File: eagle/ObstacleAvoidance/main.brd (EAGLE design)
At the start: 115 x 70 mm, 19 parts, among them IC1 L293D, X1 JST-XH-02-PIN-LONG-PAD, X2 JST-XH-02-PIN-LONG-PAD, X3 JST-XH-04-PIN-LONG-PAD

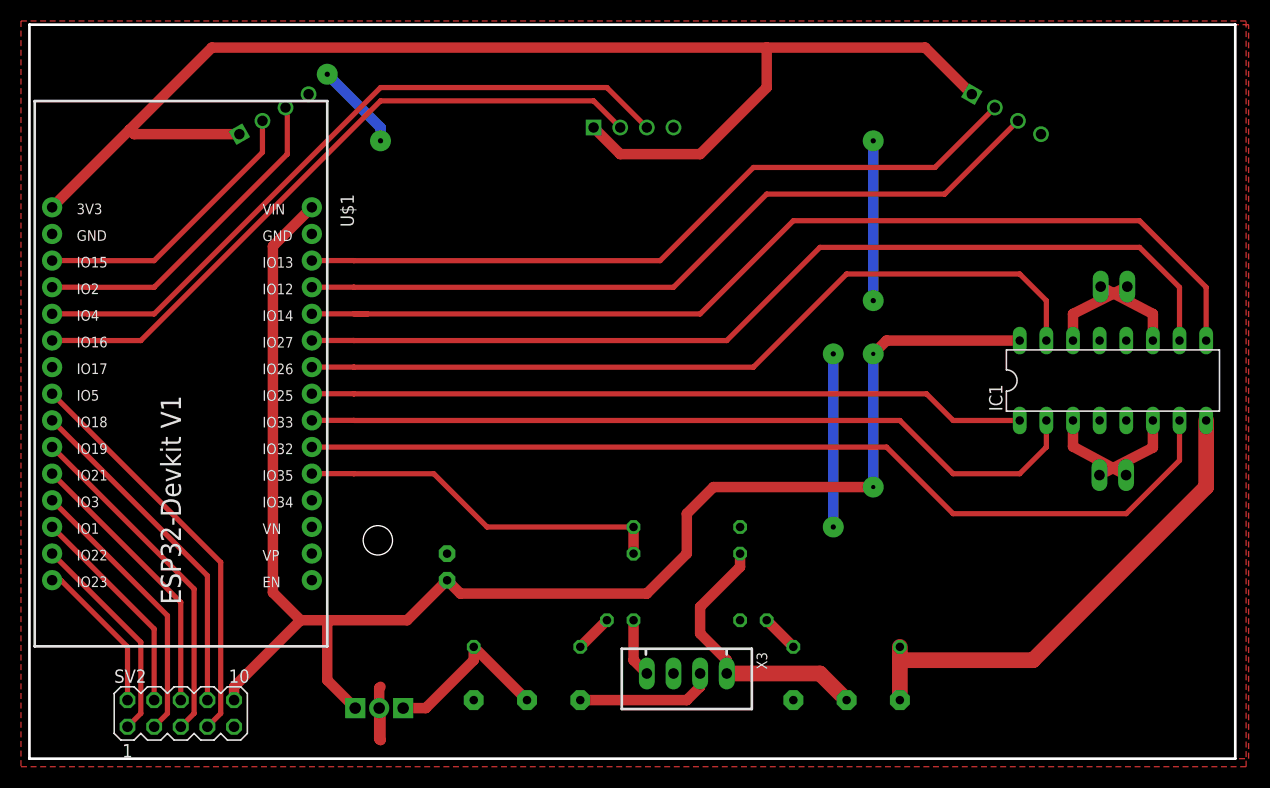
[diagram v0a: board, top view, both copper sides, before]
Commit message: Feat: New PCB routing
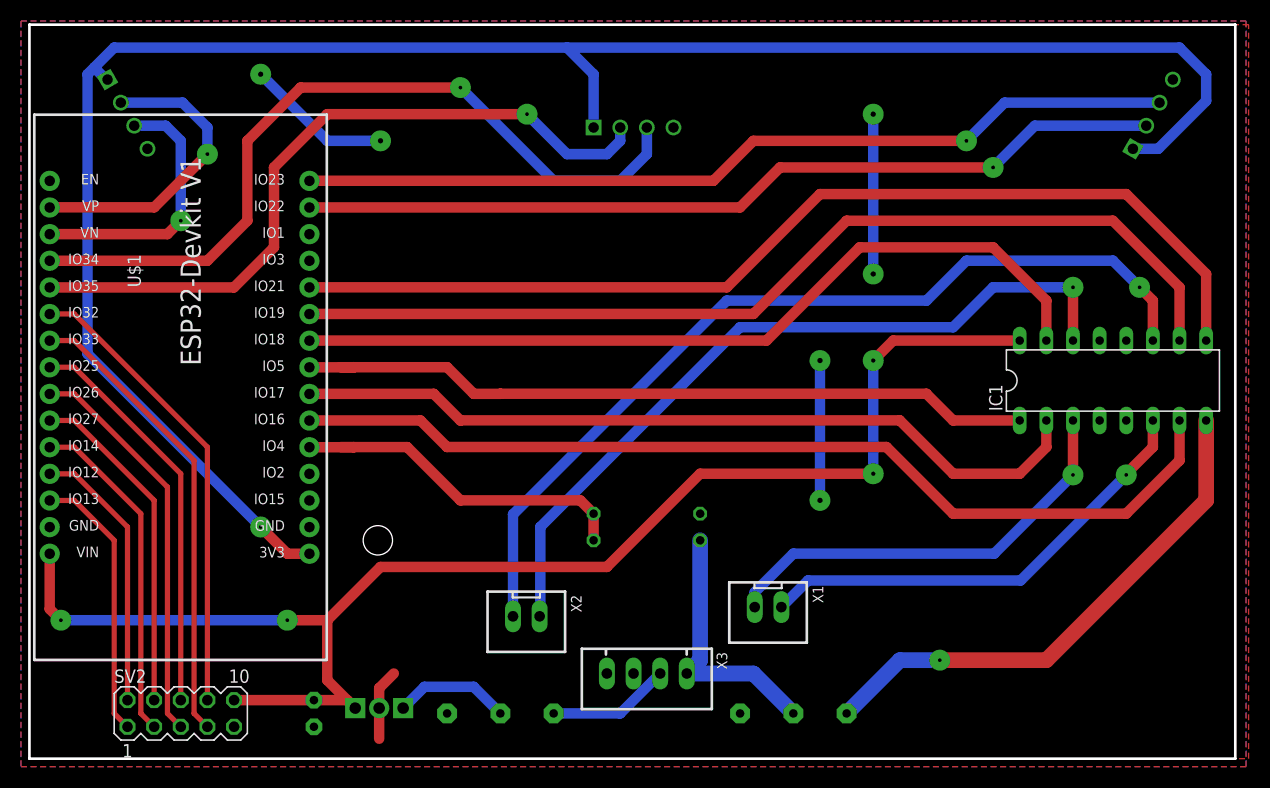
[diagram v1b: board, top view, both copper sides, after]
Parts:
- removed LED1, LED2: TLLG4400, led:LED3MM
- removed R3, R4: 1k, rcl:0207/10
- moved X2 64.3 mm to (69.8, 25.8), flipped to the top, turned to 180 degrees
- moved X1 35.2 mm to (92.8, 26.7), flipped to the top
- moved C2 18.9 mm to (49.5, 16.5), turned to 270 degrees
- moved U$2 14.0 mm to (129.5, 73.7), turned to 120 degrees
- moved U$3 14.0 mm to (31.8, 73.7), turned to 240 degrees
- moved U$1 13.0 mm to (35.6, 54.6), turned to 90 degrees
- moved J2 5.24 mm to (92.7, 16.5)
- moved R1 4.02 mm to (81.3, 35.6)
- moved R2 4.02 mm to (81.3, 33.0)
- moved X3 3.81 mm to (81.3, 20.3)
- moved J1 2.84 mm to (64.8, 16.5)
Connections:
- removed net N$15: U$1.7
- removed net N$5: LED1.A, R4.1
- removed net N$9: LED2.A, R3.2
- net 12V-VCC2: no longer R3.1
- net 8V-1: no longer R4.2
- net ECHO-F: now also U$1.19; no longer U$1.5
- net ECHO-L: now also U$1.18; no longer U$1.4
- net ECHO-R: now also U$1.15; no longer U$1.27
- net GND: no longer LED1.K, LED2.K
- net IN1-A: now also U$1.10; no longer U$1.25
- net IN1-B: now also U$1.6; no longer U$1.21
- net IN2-A: now also U$1.9; no longer U$1.24
- net IN2-B: now also U$1.7; no longer U$1.22
- net OUT1: now also U$1.27; no longer U$1.15
- net OUT2: now also U$1.28; no longer U$1.14
- net OUT3: now also U$1.25; no longer U$1.13
- net OUT4: now also U$1.26; no longer U$1.12
- net OUT5: now also U$1.23; no longer U$1.11
- net OUT6: now also U$1.24; no longer U$1.10
- net OUT7: now also U$1.21; no longer U$1.9
- net OUT8: now also U$1.22; no longer U$1.8
- net PWM-A: now also U$1.11; no longer U$1.26
- net PWM-B: now also U$1.8; no longer U$1.23
- net TRIG-F: now also U$1.20; no longer U$1.6
- net TRIG-L: now also U$1.17; no longer U$1.3
- net TRIG-R: now also U$1.14; no longer U$1.28
- net VOLT: now also U$1.5; no longer U$1.20
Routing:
- net N$4: track 8.16 -> 86.2 mm, vias 0 -> 1
- net N$3: track 8.34 -> 73.9 mm, vias 0 -> 1
- net 3.3V: track 130.5 -> 186.3 mm, vias 0 -> 1
- net N$2: track 8.32 -> 44.4 mm, vias 0 -> 1
- net N$1: track 8.24 -> 41.6 mm, vias 0 -> 1
- net 5V: track 152.1 -> 137.0 mm, vias 2 -> 4
- net TRIG-R: track 71.2 -> 83.0 mm, vias 0 -> 1
- net OUT3: track 20.6 -> 32.2 mm
- net OUT5: track 26.7 -> 38.3 mm
- net OUT7: track 32.8 -> 44.4 mm
- net OUT1: track 14.9 -> 26.0 mm
- net ECHO-R: track 73.9 -> 84.2 mm, vias 0 -> 1
- net ECHO-F: track 67.2 -> 75.5 mm, vias 0 -> 1
- net ECHO-L: track 32.2 -> 25.7 mm, vias 0 -> 1
- net 8V-1: track 17.1 -> 11.2 mm
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- added copper zone on layer 16, net GND

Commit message: Feat: Swap bottom-top
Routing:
- net IN2-B: track 77.0 -> 74.2 mm
- net 5V: track 137.0 -> 134.5 mm
- net N$3: track 73.9 -> 75.6 mm
- net 8V: track 11.7 -> 13.2 mm
- net OUT6: track 38.3 -> 36.9 mm
- net OUT3: track 32.2 -> 30.8 mm
- net OUT4: track 32.2 -> 30.8 mm
- net OUT2: track 26.0 -> 24.7 mm
- net OUT1: track 26.0 -> 24.7 mm
- net OUT7: track 44.4 -> 43.0 mm
- net OUT5: track 38.3 -> 36.9 mm
- net OUT8: track 44.4 -> 43.0 mm
- net PWM-B: track 71.1 -> 69.8 mm
- net VOLT: track 33.5 -> 32.3 mm
- net IN1-B: track 92.6 -> 91.5 mm
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
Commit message: Feat: 3D model and pcb changes
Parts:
- moved U$2 2.54 mm to (129.5, 76.2)
- moved U$3 2.54 mm to (31.8, 76.2)
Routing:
- net 3.3V: track 185.9 -> 190.8 mm
- net ECHO-L: track 25.7 -> 27.5 mm
- net ECHO-R: track 84.2 -> 86.0 mm
- net TRIG-R: track 83.0 -> 84.1 mm
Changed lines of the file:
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@@
 </layers>
 <board>
-<fusionsync huburn="a.YnVzaW5lc3M6Z21haWw0MzYwOTY" projecturn="a.YnVzaW5lc3M6Z21haWw0MzYwOTYjMjAxOTExMjUyNDE4MzY5NzY" f3durn="urn:adsk.wipprod:dm.lineage:NBSkxh8rSPakSfSzdT5ugQ" pcbguid="deb97233-5946-44c7-9ab5-95046c2ec4ee" lastpulledtime="2019-11-27T21:35:54Z" lastsyncedchangeguid="d6366f3e-85ad-fa97-e8cb-b64b5bb49a39"/>
+<fusionsync huburn="a.YnVzaW5lc3M6Z21haWw0MzYwOTY" projecturn="a.YnVzaW5lc3M6Z21haWw0MzYwOTYjMjAxOTExMjUyNDE4MzY5NzY" f3durn="urn:adsk.wipprod:dm.lineage:NBSkxh8rSPakSfSzdT5ugQ" pcbguid="deb97233-5946-44c7-9ab5-95046c2ec4ee" lastpulledtime="2019-11-29T17:32:53Z" lastsyncedchangeguid="fbe9b0a7-f74d-2411-8d66-78c79ab0fd07"/>
 <plain>
+<hole x="42.397" y="77.197" drill="4"/>
+<hole x="117.397" y="77.197" drill="4"/>
+<hole x="80" y="77.197" drill="4"/>
 <wire x1="22.397" y1="82.197" x2="22.397" y2="12.197" width="0.254" layer="20"/>
 <wire x1="22.397" y1="12.197" x2="137.397" y2="12.197" width="0.254" layer="20"/>
@@
 <attribute name="VALUE" x="118.237" y="47.625" size="1.27" layer="27" ratio="10"/>
 </element>
-<element name="U$2" library="diy-modules" package="ULTRASONIC-HC-SR04#V" value="ULTRASONIC-HC-SR04#V" x="129.54" y="73.66" smashed="yes" rot="MR120">
-<attribute name="NAME" x="125.690515625" y="75.88249375" size="1.27" layer="26" rot="MR120" align="bottom-center"/>
-<attribute name="VALUE" x="113.592140625" y="82.86749375" size="1.27" layer="28" rot="MR120" align="top-center"/>
-</element>
-<element name="U$3" library="diy-modules" package="ULTRASONIC-HC-SR04#V" value="ULTRASONIC-HC-SR04#V" x="31.75" y="73.66" smashed="yes" rot="MR240">
-<attribute name="NAME" x="30.10020625" y="72.7075" size="1.27" layer="26" rot="MR210" align="bottom-center"/>
-<attribute name="VALUE" x="47.69785" y="82.86749375" size="1.27" layer="28" rot="MR240" align="top-center"/>
+<element name="U$2" library="diy-modules" package="ULTRASONIC-HC-SR04#V" value="ULTRASONIC-HC-SR04#V" x="129.54" y="76.2" smashed="yes" rot="MR120">
+<attribute name="NAME" x="125.690515625" y="78.42249375" size="1.27" layer="26" rot="MR120" align="bottom-center"/>
+<attribute name="VALUE" x="113.592140625" y="85.40749375" size="1.27" layer="28" rot="MR120" align="top-center"/>
+</element>
+<element name="U$3" library="diy-modules" package="ULTRASONIC-HC-SR04#V" value="ULTRASONIC-HC-SR04#V" x="31.75" y="76.2" smashed="yes" rot="MR240">
+<attribute name="NAME" x="30.10020625" y="75.2475" size="1.27" layer="26" rot="MR210" align="bottom-center"/>
+<attribute name="VALUE" x="47.69785" y="85.40749375" size="1.27" layer="28" rot="MR240" align="top-center"/>
 </element>
 <element name="U$7" library="tango" package="L7805" value="-L7805" x="55.88" y="26.67" smashed="yes" rot="MR0">
@@
 <wire x1="102.87" y1="73.66" x2="102.87" y2="58.42" width="1" layer="1"/>
 <wire x1="97.79" y1="50.165" x2="97.79" y2="36.83" width="1" layer="1"/>
-<wire x1="127" y1="52.07" x2="131.445" y2="76.95955625" width="0" layer="19" extent="1-1"/>
-<wire x1="124.46" y1="52.07" x2="127" y2="52.07" width="0" layer="19" extent="1-1"/>
-<wire x1="127" y1="44.45" x2="127" y2="52.07" width="0" layer="19" extent="1-1"/>
-<wire x1="124.46" y1="44.45" x2="127" y2="44.45" width="0" layer="19" extent="1-1"/>
-<wire x1="102.87" y1="58.42" x2="124.46" y2="52.07" width="0" layer="19" extent="1-1"/>
-<wire x1="97.79" y1="50.165" x2="102.87" y2="58.42" width="0" layer="19" extent="1-1"/>
-<wire x1="86.36" y1="35.56" x2="97.79" y2="36.83" width="0" layer="19" extent="1-1"/>
-<wire x1="77.47" y1="20.32" x2="86.36" y2="35.56" width="0" layer="19" extent="1-1"/>
-<wire x1="83.82" y1="72.39" x2="102.87" y2="73.66" width="0" layer="19" extent="1-1"/>
-<wire x1="57.15" y1="20.32" x2="77.47" y2="20.32" width="0" layer="19" extent="1-1"/>
-<wire x1="49.53" y1="15.24" x2="55.753" y2="14.097" width="0" layer="19" extent="1-1"/>
-<wire x1="41.91" y1="15.24" x2="49.53" y2="15.24" width="0" layer="19" extent="1-1"/>
-<wire x1="24.33" y1="34.28" x2="41.91" y2="15.24" width="0" layer="19" extent="1-1"/>
-<wire x1="55.88" y1="71.12" x2="83.82" y2="72.39" width="0" layer="19" extent="1-1"/>
-<wire x1="33.655" y1="70.360440625" x2="44.45" y2="77.47" width="0" layer="19" extent="1-1"/>
 </signal>
 <signal name="5V">
@@
 <contactref element="U$8" pad="1"/>
 <via x="44.45" y="34.29" extent="1-16" drill="0.35" diameter="2"/>
-<wire x1="29.845" y1="76.95955625" x2="29.72044375" y2="76.95955625" width="1" layer="16"/>
+<wire x1="29.845" y1="79.49955625" x2="29.72044375" y2="79.49955625" width="1" layer="16"/>
 <wire x1="49.1" y1="31.74" x2="47" y2="31.74" width="1" layer="16"/>
 <wire x1="47" y1="31.74" x2="44.45" y2="34.29" width="1" layer="16"/>
 <wire x1="44.45" y1="34.29" x2="27.94" y2="50.8" width="1" layer="1"/>
-<wire x1="27.94" y1="50.8" x2="27.94" y2="77.47" width="1" layer="1"/>
-<wire x1="27.94" y1="77.47" x2="30.48" y2="80.01" width="1" layer="1"/>
-<wire x1="132.08" y1="80.01" x2="134.62" y2="77.47" width="1" layer="1"/>
-<wire x1="134.62" y1="77.47" x2="134.62" y2="73.66" width="1" layer="1"/>
-<wire x1="134.62" y1="73.66" x2="130.81" y2="69.85" width="1" layer="1"/>
-<wire x1="130.81" y1="69.85" x2="128.145440625" y2="69.85" width="1" layer="1"/>
-<wire x1="128.145440625" y1="69.85" x2="127.635" y2="70.360440625" width="1" layer="1"/>
-<wire x1="30.48" y1="80.01" x2="73.66" y2="80.01" width="1" layer="1"/>
-<wire x1="73.66" y1="80.01" x2="132.08" y2="80.01" width="1" layer="1"/>
-<wire x1="73.66" y1="80.01" x2="76.2" y2="77.47" width="1" layer="1"/>
+<wire x1="27.94" y1="77.47" x2="27.94" y2="50.8" width="1" layer="1"/>
+<wire x1="132.08" y1="81.28" x2="134.62" y2="78.74" width="1" layer="1"/>
+<wire x1="134.62" y1="78.74" x2="134.62" y2="76.2" width="1" layer="1"/>
+<wire x1="134.62" y1="76.2" x2="131.320440625" y2="72.900440625" width="1" layer="1"/>
+<wire x1="72.39" y1="81.28" x2="29.21" y2="81.28" width="1" layer="1"/>
+<wire x1="72.39" y1="81.28" x2="132.08" y2="81.28" width="1" layer="1"/>
+<wire x1="72.39" y1="81.28" x2="76.2" y2="77.47" width="1" layer="1"/>
 <wire x1="76.2" y1="77.47" x2="76.2" y2="72.39" width="1" layer="1"/>
-<wire x1="44.45" y1="34.29" x2="29.845" y2="76.95955625" width="0" layer="19" extent="1-1"/>
+<wire x1="27.877721875" y1="77.532278125" x2="27.94" y2="77.47" width="1" layer="1"/>
+<wire x1="29.21" y1="81.28" x2="27.877721875" y2="79.947721875" width="1" layer="1"/>
+<wire x1="29.845" y1="79.49955625" x2="27.877721875" y2="77.532278125" width="1" layer="1"/>
+<wire x1="27.877721875" y1="77.532278125" x2="27.877721875" y2="79.947721875" width="1" layer="1"/>
+<wire x1="127.635" y1="72.900440625" x2="131.320440625" y2="72.900440625" width="1" layer="1"/>
 </signal>
 <signal name="VOLT">
@@
 <wire x1="36.83" y1="63.5" x2="35.55" y2="62.22" width="1" layer="16"/>
 <wire x1="35.55" y1="62.22" x2="24.33" y2="62.22" width="1" layer="16"/>
-<wire x1="36.83" y1="63.5" x2="36.83" y2="71.12" width="1" layer="1"/>
-<wire x1="35.389853125" y1="72.560146875" x2="32.385" y2="72.560146875" width="1" layer="1"/>
-<wire x1="36.83" y1="71.12" x2="35.389853125" y2="72.560146875" width="1" layer="1"/>
+<wire x1="36.83" y1="63.5" x2="36.83" y2="66.04" width="1" layer="1"/>
+<wire x1="31.115" y1="73.830146875" x2="32.385" y2="75.100146875" width="1" layer="1"/>
+<wire x1="31.115" y1="73.830146875" x2="31.115" y2="71.755" width="1" layer="1"/>
+<wire x1="36.83" y1="66.04" x2="31.115" y2="71.755" width="1" layer="1"/>
 </signal>
 <signal name="TRIG-L">
@@
 <wire x1="24.33" y1="64.76" x2="34.28" y2="64.76" width="1" layer="16"/>
 <wire x1="34.28" y1="64.76" x2="39.37" y2="69.85" width="1" layer="16"/>
-<wire x1="31.115" y1="74.75985" x2="37.00015" y2="74.75985" width="1" layer="1"/>
-<wire x1="39.37" y1="72.39" x2="39.37" y2="69.85" width="1" layer="1"/>
-<wire x1="37.00015" y1="74.75985" x2="39.37" y2="72.39" width="1" layer="1"/>
+<wire x1="31.115" y1="77.29985" x2="33.19015" y2="77.29985" width="1" layer="1"/>
+<wire x1="39.37" y1="71.12" x2="39.37" y2="69.85" width="1" layer="1"/>
+<wire x1="39.37" y1="71.12" x2="33.19015" y2="77.29985" width="1" layer="1"/>
 </signal>
 <signal name="ECHO-R">
@@
 <wire x1="87.62" y1="67.3" x2="91.44" y2="71.12" width="1" layer="16"/>
 <wire x1="91.44" y1="71.12" x2="111.76" y2="71.12" width="1" layer="16"/>
-<wire x1="111.76" y1="71.12" x2="115.39985" y2="74.75985" width="1" layer="1"/>
-<wire x1="115.39985" y1="74.75985" x2="130.175" y2="74.75985" width="1" layer="1"/>
+<wire x1="113.03" y1="73.66" x2="111.76" y2="72.39" width="1" layer="1"/>
+<wire x1="111.76" y1="71.12" x2="111.76" y2="72.39" width="1" layer="1"/>
+<wire x1="130.175" y1="77.29985" x2="127.472225" y2="77.29985" width="1" layer="1"/>
+<wire x1="123.832375" y1="73.66" x2="113.03" y2="73.66" width="1" layer="1"/>
+<wire x1="127.472225" y1="77.29985" x2="123.832375" y2="73.66" width="1" layer="1"/>
 </signal>
 <signal name="TRIG-R">
@@
 <wire x1="49.1" y1="64.76" x2="88.89" y2="64.76" width="1" layer="16"/>
 <wire x1="92.71" y1="68.58" x2="114.3" y2="68.58" width="1" layer="16"/>
-<wire x1="114.3" y1="68.58" x2="118.280146875" y2="72.560146875" width="1" layer="1"/>
-<wire x1="118.280146875" y1="72.560146875" x2="128.905" y2="72.560146875" width="1" layer="1"/>
+<wire x1="114.3" y1="68.58" x2="120.65" y2="68.58" width="1" layer="1"/>
+<wire x1="127.170146875" y1="75.100146875" x2="120.65" y2="68.58" width="1" layer="1"/>
+<wire x1="127.170146875" y1="75.100146875" x2="128.905" y2="75.100146875" width="1" layer="1"/>
 </signal>
 <signal name="TRIG-F">
